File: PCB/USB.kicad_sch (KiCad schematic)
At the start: 0 parts

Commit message: Update Power schematic with new symbols and components
Replaced and added several symbols in Power.kicad_sch, including MCP73831-2-OT battery charger, TPS61090 boost converter, and updated passive components (LED, capacitor, inductor, resistor). Adjusted symbol properties, footprints, and pinouts to match new components. Updated schematic text, junctions, and added descriptive notes for charge rate and low battery voltage. Minor tweaks to MusicPlayer.kicad_sch sheet positions and grouping in MusicPlayer.kicad_pro.
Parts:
- added J2: USB_C_Receptacle_USB2.0_16P, Connector_USB:USB_C_Receptacle_G-Switch_GT-USB-7010ASV, symbol Connector:USB_C_Receptacle_USB2.0_16P
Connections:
- new net GND: J2.A1 (GND), J2.A12 (GND), J2.B1 (GND), J2.B12 (GND), J2.S1 (SHIELD)
- new net VBUS: J2.A4 (VBUS), J2.A9 (VBUS), J2.B4 (VBUS), J2.B9 (VBUS)
- no-connect marks 0 -> 8

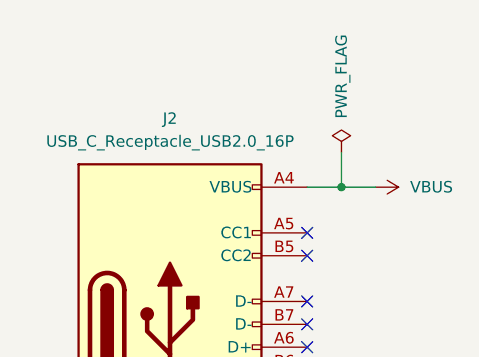
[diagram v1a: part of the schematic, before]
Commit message: Add components & update KiCad schematic settings
Add and refine schematic symbols and project settings across PCB files. Inputs.kicad_sch: expand library symbols and instances (resistor, SPDT switch, power flags, GND, wiring and global labels). Power.kicad_sch: add a Schottky diode symbol, replace/regenerate regulator symbol (rename to LD1117S33TR_SOT223 and update datasheet/description/keywords), and add simulation transistor symbols (NMOS, PNP) with Sim.* properties and updated graphics. MusicPlayer.kicad_pro: tighten lib_symbol_mismatch to error, adjust BOM settings (exclude_dnp true, show quantity, hide DNP/Exclude fields, add/hide Sim.Device/Sim.Type fields) and change BOM sorting to Reference ascending. These changes improve symbol definitions for simulation, ERC/BOM accuracy, and project export settings.
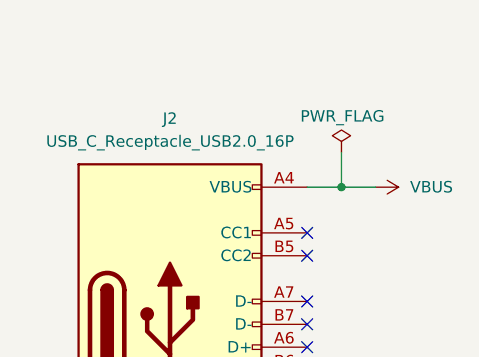
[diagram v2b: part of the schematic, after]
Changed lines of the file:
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@@
+	(wire
+		(pts
+			(xy 67.31 78.74) (xy 71.12 78.74)
+		)
+		(stroke
+			(width 0)
+			(type default)
+		)
+	)
+	(wire
+		(pts
+			(xy 67.31 78.74) (xy 67.31 74.93)
+		)
+		(stroke
+			(width 0)
+			(type default)
+		)
+	)
 	(wire
 		(pts
@@
 	(wire
 		(pts
-			(xy 67.31 78.74) (xy 67.31 74.93)
-		)
-		(stroke
-			(width 0)
-			(type default)
-		)
-	)
-	(wire
-		(pts
 			(xy 40.64 116.84) (xy 40.64 120.65)
-		)
-		(stroke
-			(width 0)
-			(type default)
-		)
-	)
-	(wire
-		(pts
-			(xy 67.31 78.74) (xy 71.12 78.74)
 		)
 		(stroke
@@
 		(on_board yes)
 		(dnp no)
-		(fields_autoplaced yes)
-		(property "Reference" "#FLG02"
+		(property "Reference" "#FLG03"
 			(at 67.31 73.025 0)
 			(effects
@@
 		)
 		(property "Value" "PWR_FLAG"
-			(at 67.3099 71.12 90)
+			(at 62.738 70.866 0)
 			(effects
 				(font
@@
 			(project "MusicPlayer"
 				(path "/2c2d2da5-7991-4e93-87f2-9633b55e39cf/87fde085-6ff4-4e87-8cdf-89f94cb0cfa0"
-					(reference "#FLG02")
+					(reference "#FLG03")
 					(unit 1)
 				)

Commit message: Finished the schematic.
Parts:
- added C17: 10u, Capacitor_SMD:C_0201_0603Metric, symbol Device:C
- added C18, C19, C20, C21, C22: 100n, Capacitor_SMD:C_0201_0603Metric, symbol Device:C
- added R24, R25: 5.1k, Resistor_SMD:R_0201_0603Metric, symbol Device:R
- added U7: USBLC6-2P6, Package_TO_SOT_SMD:SOT-666, symbol Power_Protection:USBLC6-2P6
- added U8: CH340C, Package_SO:SOIC-16_3.9x9.9mm_P1.27mm, symbol Interface_USB:CH340C
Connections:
- net GND: now also C17.1, C18.1, C19.1, C20.2, C21.2, C22.2, R24.2, R25.1, U7.2 (GND), U8.1 (GND)
- net VBUS: now also C17.2, C18.2, C19.2, C20.1, U7.5 (VBUS)
- net at J2.A5 (CC1): now also R24.1
- net at J2.A6 (D+): now also J2.B6 (D+), U7.3 (I/O2)
- net at J2.A7 (D-): now also J2.B7 (D-), U7.1 (I/O1)
- net at J2.B5 (CC2): now also R25.2
- new net: C22.1, U8.4 (V3)
- new net +3V3: C21.1, U8.16 (VCC)
- new net D+: U7.4 (I/O2), U8.5 (UD+)
- new net D-: U7.6 (I/O1), U8.6 (UD-)
- new net RX: U8.2 (TXD)
- new net TX: U8.3 (RXD)
- no-connect marks 8 -> 9

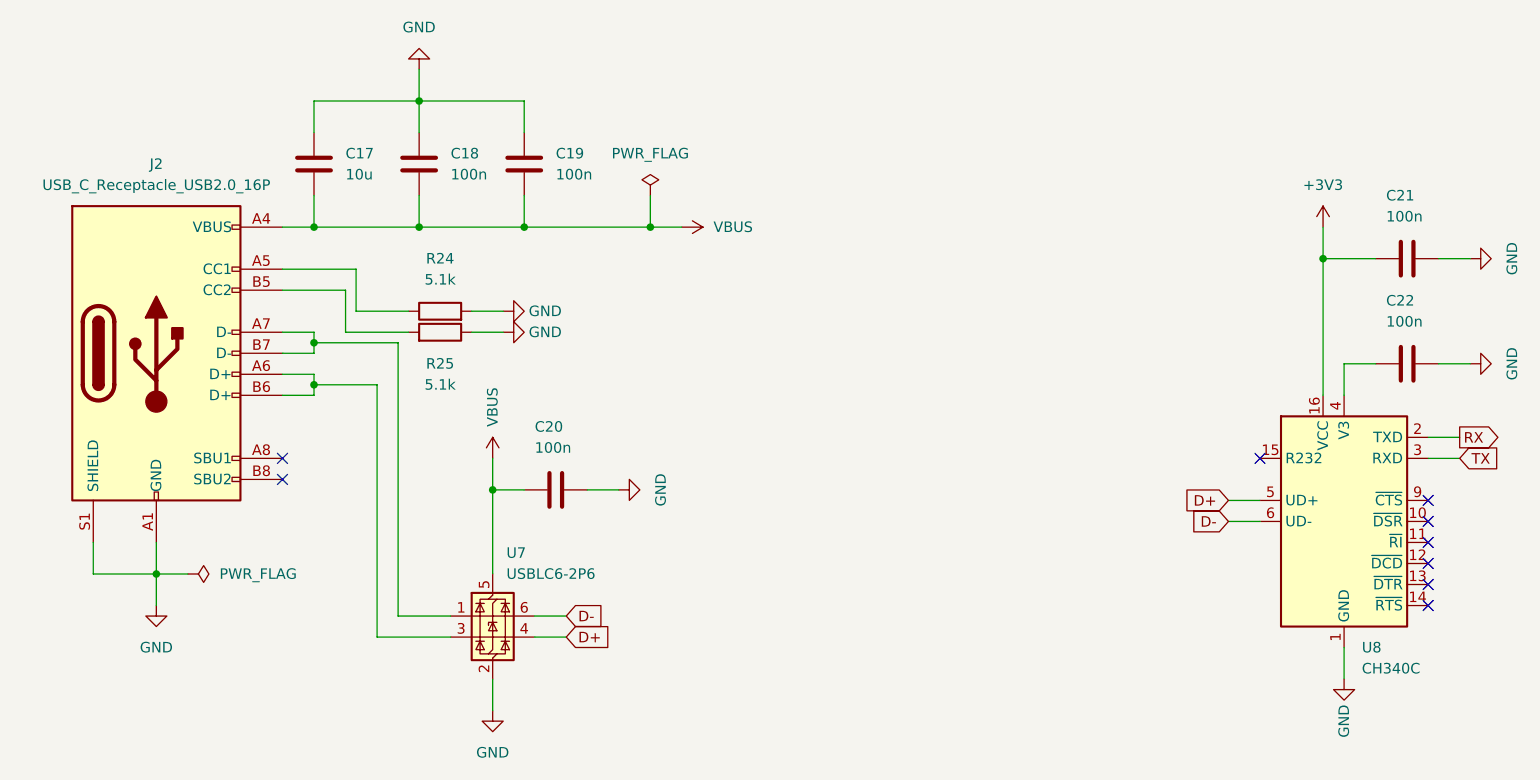
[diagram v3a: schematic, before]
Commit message: Finale touch up on schematics
Added net classes and did set the pcb configuration values.
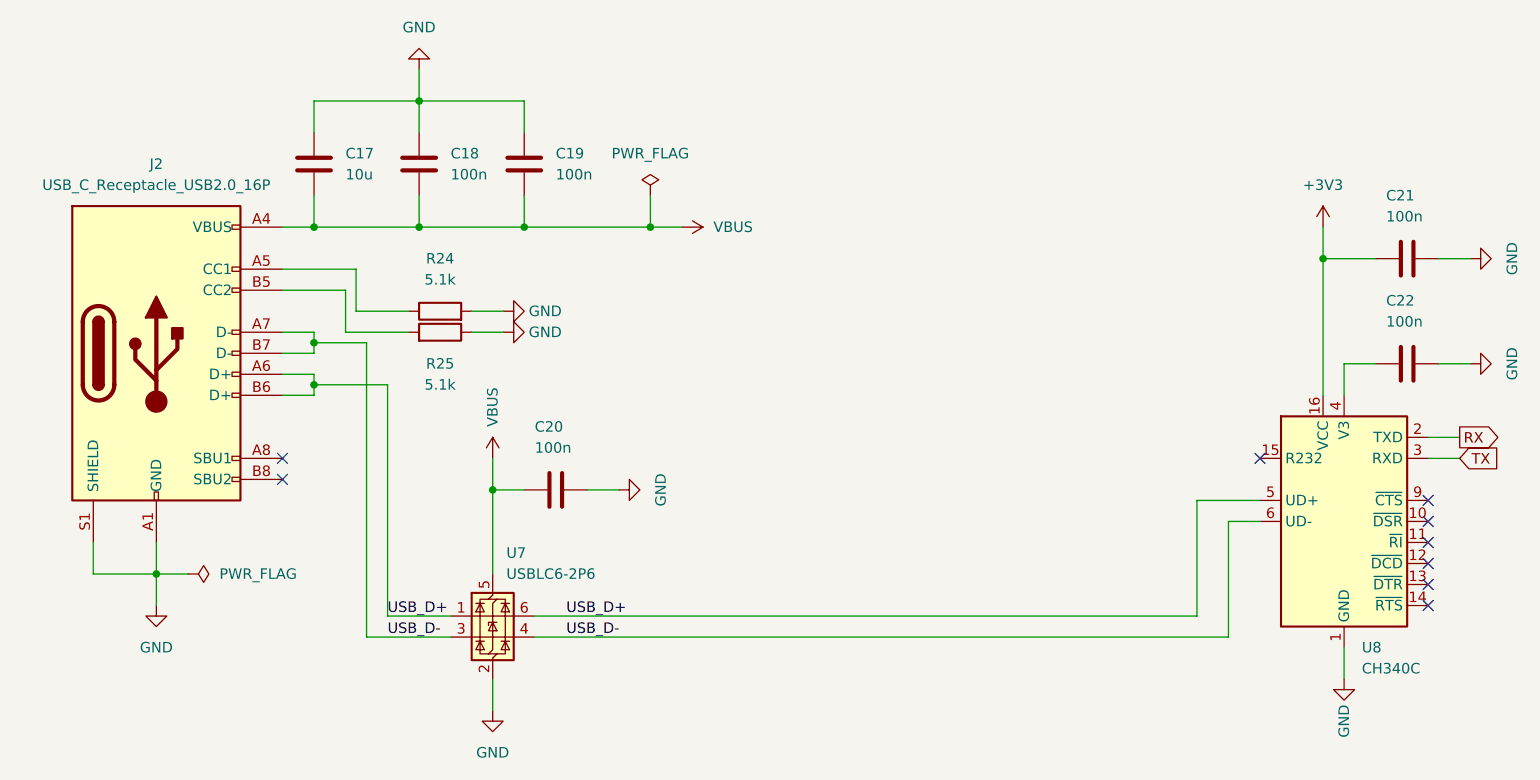
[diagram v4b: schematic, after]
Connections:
- net USB_D+: now reaches J2.A6 (D+), J2.B6 (D+)
- net USB_D+: now also U7.1 (I/O1), U7.6 (I/O1), U8.5 (UD+); no longer U7.3 (I/O2)
- net USB_D-: now reaches J2.A7 (D-), J2.B7 (D-)
- net USB_D-: now also U7.3 (I/O2), U7.4 (I/O2), U8.6 (UD-); no longer U7.1 (I/O1)
- removed net D+: U7.4 (I/O2), U8.5 (UD+)
- removed net D-: U7.6 (I/O1), U8.6 (UD-)

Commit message: fixed schematic errors
Accidentally set all SMD 0603 to SMD 0603 metric
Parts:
- C17, C18, C19, C20, C21, C22: footprint Capacitor_SMD:C_0201_0603Metric -> Capacitor_SMD:C_0603_1608Metric
- J2: LCSC C2988369 -> (none)
- R24, R25: footprint Resistor_SMD:R_0201_0603Metric -> Resistor_SMD:R_0603_1608Metric
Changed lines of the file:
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@@
-	)
-	(symbol
-		(lib_id "Connector:USB_C_Receptacle_USB2.0_16P")
-		(at 48.26 93.98 0)
-		(unit 1)
-		(exclude_from_sim no)
-		(in_bom yes)
-		(on_board yes)
-		(dnp no)
-		(property "Reference" "J2"
-			(at 48.26 71.12 0)
-			(effects
-				(font
-					(size 1.27 1.27)
-				)
-			)
-		)
-		(property "Value" "USB_C_Receptacle_USB2.0_16P"
-			(at 48.26 73.66 0)
-			(effects
-				(font
-					(size 1.27 1.27)
-				)
-			)
-		)
-		(property "Footprint" "Connector_USB:USB_C_Receptacle_G-Switch_GT-USB-7010ASV"
-			(at 52.07 93.98 0)
-			(effects
-				(font
-					(size 1.27 1.27)
-				)
-				(hide yes)
-			)
-		)
-		(property "Datasheet" "https://www.usb.org/sites/default/files/documents/usb_type-c.zip"
-			(at 52.07 93.98 0)
-			(effects
-				(font
-					(size 1.27 1.27)
-				)
-				(hide yes)
-			)
-		)
-		(property "Description" "USB 2.0-only 16P Type-C Receptacle connector"
-			(at 48.26 93.98 0)
-			(effects
-				(font
-					(size 1.27 1.27)
-				)
-				(hide yes)
-			)
-		)
-		(property "LCSC" "C2988369"
-			(at 48.26 93.98 0)
-			(effects
-				(font
-					(size 1.27 1.27)
-				)
-				(hide yes)
-			)
-		)
-		(pin "A6"
-		)
-		(pin "S1"
-		)
-		(pin "B5"
-		)
-		(pin "A9"
-		)
-		(pin "A1"
-		)
-		(pin "B12"
-		)
-		(pin "B4"
-		)
-		(pin "B9"
-		)
-		(pin "A7"
-		)
-		(pin "A5"
-		)
-		(pin "A4"
-		)
-		(pin "B7"
-		)
-		(pin "A12"
-		)
-		(pin "B1"
-		)
-		(pin "B6"
-		)
-		(pin "A8"
-		)
-		(pin "B8"
-		)
-		(instances
-			(project ""
-				(path "/2c2d2da5-7991-4e93-87f2-9633b55e39cf/87fde085-6ff4-4e87-8cdf-89f94cb0cfa0"
-					(reference "J2")
-					(unit 1)
-				)
-			)
-		)
 	)
 	(symbol
@@
 			)
 		)
-		(property "Footprint" "Capacitor_SMD:C_0201_0603Metric"
+		(property "Footprint" "Capacitor_SMD:C_0603_1608Metric"
 			(at 80.9752 74.93 0)
 			(effects
@@
 			)
 		)
-		(property "Footprint" "Resistor_SMD:R_0201_0603Metric"
+		(property "Footprint" "Resistor_SMD:R_0603_1608Metric"
 			(at 82.55 90.678 90)
 			(effects
@@
 			)
 		)
-		(property "Footprint" "Capacitor_SMD:C_0201_0603Metric"
+		(property "Footprint" "Capacitor_SMD:C_0603_1608Metric"
 			(at 68.2752 74.93 0)
 			(effects
@@
 			)
 		)
-		(property "Footprint" "Capacitor_SMD:C_0201_0603Metric"
+		(property "Footprint" "Capacitor_SMD:C_0603_1608Metric"
 			(at 93.6752 74.93 0)
 			(effects
@@
 			)
 		)
-		(property "Footprint" "Capacitor_SMD:C_0201_0603Metric"
+		(property "Footprint" "Capacitor_SMD:C_0603_1608Metric"
 			(at 100.33 109.5248 0)
 			(effects
@@
 	)
 	(symbol
+		(lib_id "Connector:USB_C_Receptacle_USB2.0_16P")
+		(at 48.26 93.98 0)
+		(unit 1)
+		(exclude_from_sim no)
+		(in_bom yes)
+		(on_board yes)
+		(dnp no)
+		(fields_autoplaced yes)
+		(property "Reference" "J2"
+			(at 48.26 71.12 0)
+			(effects
+				(font
+					(size 1.27 1.27)
+				)
+			)
+		)
+		(property "Value" "USB_C_Receptacle_USB2.0_16P"
+			(at 48.26 73.66 0)
+			(effects
+				(font
+					(size 1.27 1.27)
+				)
+			)
+		)
+		(property "Footprint" "Connector_USB:USB_C_Receptacle_G-Switch_GT-USB-7010ASV"
+			(at 52.07 93.98 0)
+			(effects
+				(font
+					(size 1.27 1.27)
+				)
+				(hide yes)
+			)
+		)
+		(property "Datasheet" "https://www.usb.org/sites/default/files/documents/usb_type-c.zip"
+			(at 52.07 93.98 0)
+			(effects
+				(font
+					(size 1.27 1.27)
+				)
+				(hide yes)
+			)
+		)
+		(property "Description" "USB 2.0-only 16P Type-C Receptacle connector"
+			(at 48.26 93.98 0)
+			(effects
+				(font
+					(size 1.27 1.27)
+				)
+				(hide yes)
+			)
+		)
+		(pin "B9"
+		)
+		(pin "A1"
+		)
+		(pin "B12"
+		)
+		(pin "A9"
+		)
+		(pin "B4"
+		)
+		(pin "A12"
+		)
+		(pin "B1"
+		)
+		(pin "S1"
+		)
+		(pin "A4"
+		)
+		(pin "A5"
+		)
+		(pin "A6"
+		)
+		(pin "B6"
+		)
+		(pin "B5"
+		)
+		(pin "A8"
+		)
+		(pin "B8"
+		)
+		(pin "B7"
+		)
+		(pin "A7"
+		)
+		(instances
+			(project ""
+				(path "/2c2d2da5-7991-4e93-87f2-9633b55e39cf/87fde085-6ff4-4e87-8cdf-89f94cb0cfa0"
+					(reference "J2")
+					(unit 1)
+				)
+			)
+		)
+	)
+	(symbol
 		(lib_id "Device:C")
 		(at 199.39 95.25 90)
@@
 			)
 		)
-		(property "Footprint" "Capacitor_SMD:C_0201_0603Metric"
+		(property "Footprint" "Capacitor_SMD:C_0603_1608Metric"
 			(at 203.2 94.2848 0)
 			(effects
@@
 			)
 		)
-		(property "Footprint" "Resistor_SMD:R_0201_0603Metric"
+		(property "Footprint" "Resistor_SMD:R_0603_1608Metric"
 			(at 82.55 93.218 90)
 			(effects
@@
 			)
 		)
-		(property "Footprint" "Capacitor_SMD:C_0201_0603Metric"
+		(property "Footprint" "Capacitor_SMD:C_0603_1608Metric"
 			(at 203.2 81.5848 0)
 			(effects

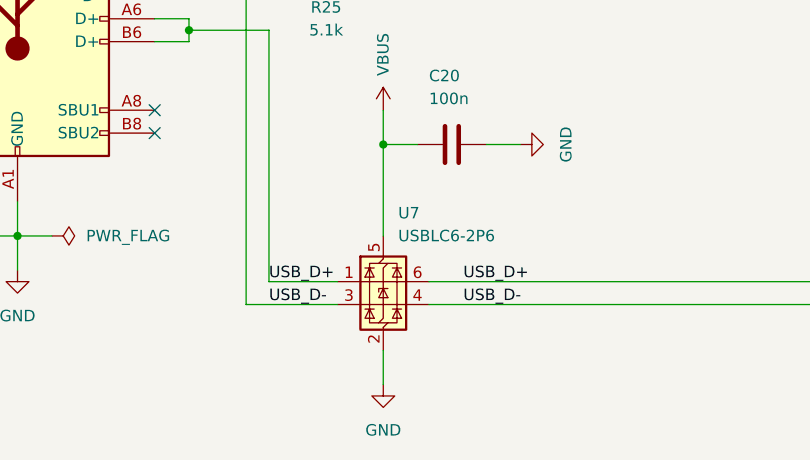
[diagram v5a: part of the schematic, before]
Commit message: Finished initial pcb routing
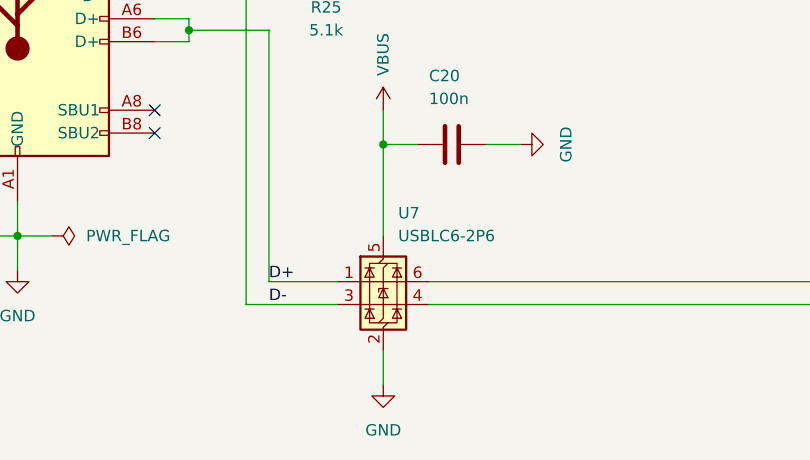
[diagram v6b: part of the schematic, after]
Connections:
- net USB_D+ renamed D+
- net D+: no longer U7.6 (I/O1), U8.5 (UD+)
- net USB_D- renamed D-
- net D-: no longer U7.4 (I/O2), U8.6 (UD-)
- new net: U7.6 (I/O1), U8.5 (UD+)
- new net: U7.4 (I/O2), U8.6 (UD-)
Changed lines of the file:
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@@
 		)
 	)
-	(label "USB_D+"
-		(at 97.79 125.73 0)
-		(effects
-			(font
-				(size 1.27 1.27)
-			)
-			(justify left bottom)
-		)
-	)
-	(label "USB_D-"
-		(at 97.79 128.27 0)
-		(effects
-			(font
-				(size 1.27 1.27)
-			)
-			(justify left bottom)
-		)
-	)
-	(label "USB_D+"
+	(label "D+"
 		(at 76.2 125.73 0)
 		(effects
@@
 		)
 	)
-	(label "USB_D-"
+	(label "D-"
 		(at 76.2 128.27 0)
 		(effects

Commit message: Finished making a PCB for it
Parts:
- J2: LCSC (none) -> C2988369
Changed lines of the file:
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@@
+			)
+		)
+		(property "LCSC" "C2988369"
+			(at 48.26 93.98 0)
+			(effects
+				(font
+					(size 1.27 1.27)
+				)
+				(hide yes)
 			)
 		)
